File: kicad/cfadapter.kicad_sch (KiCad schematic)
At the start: 5 parts, among them CON1 CF-CARD, J1 Extension port, U1 GAL16V8

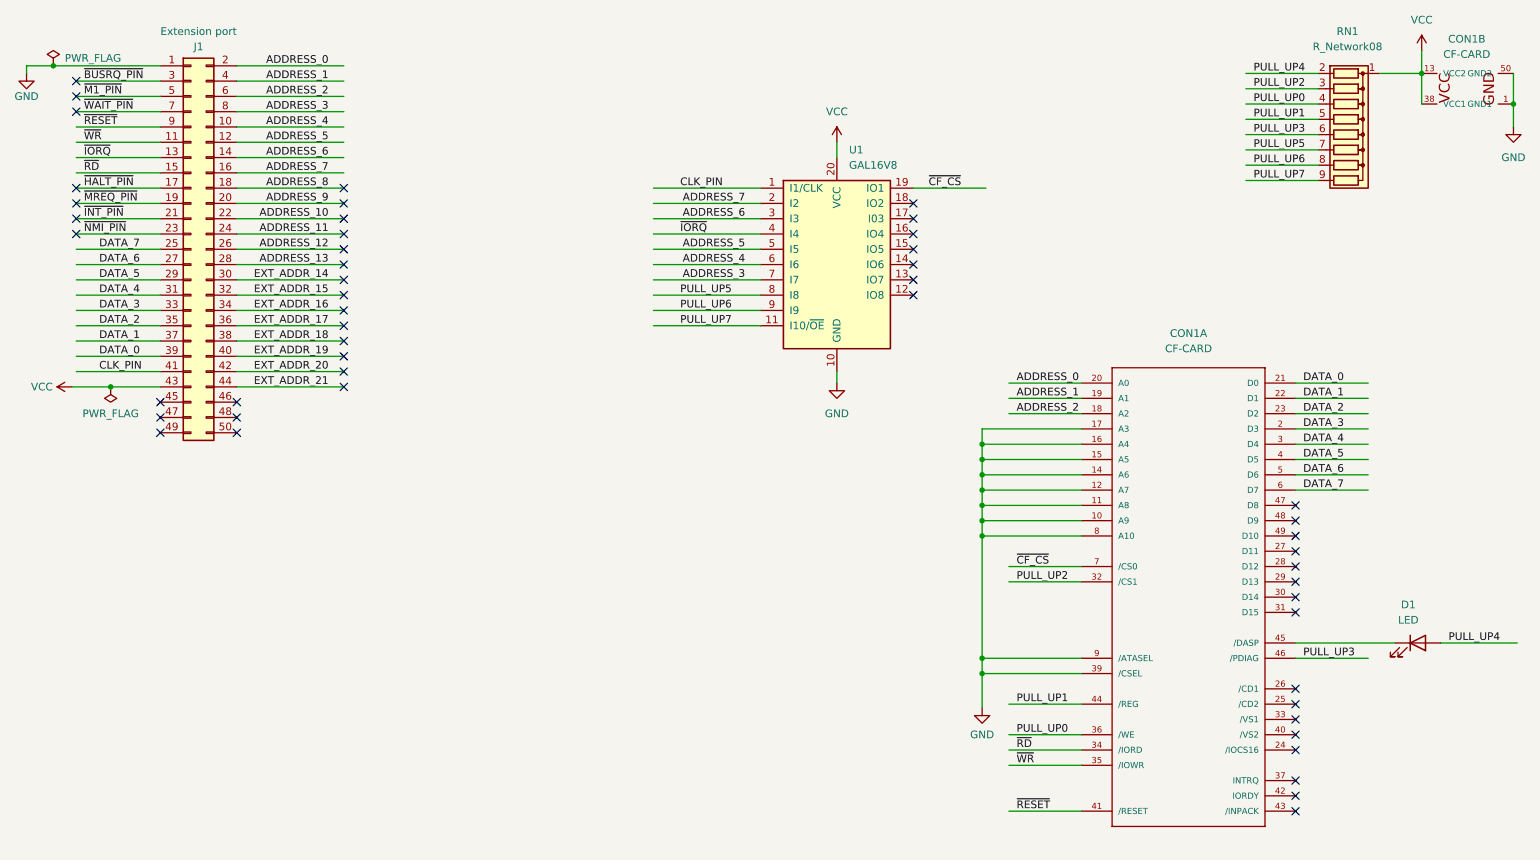
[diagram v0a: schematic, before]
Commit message: kicad: Update the PCB to the manufactured v1.0.0
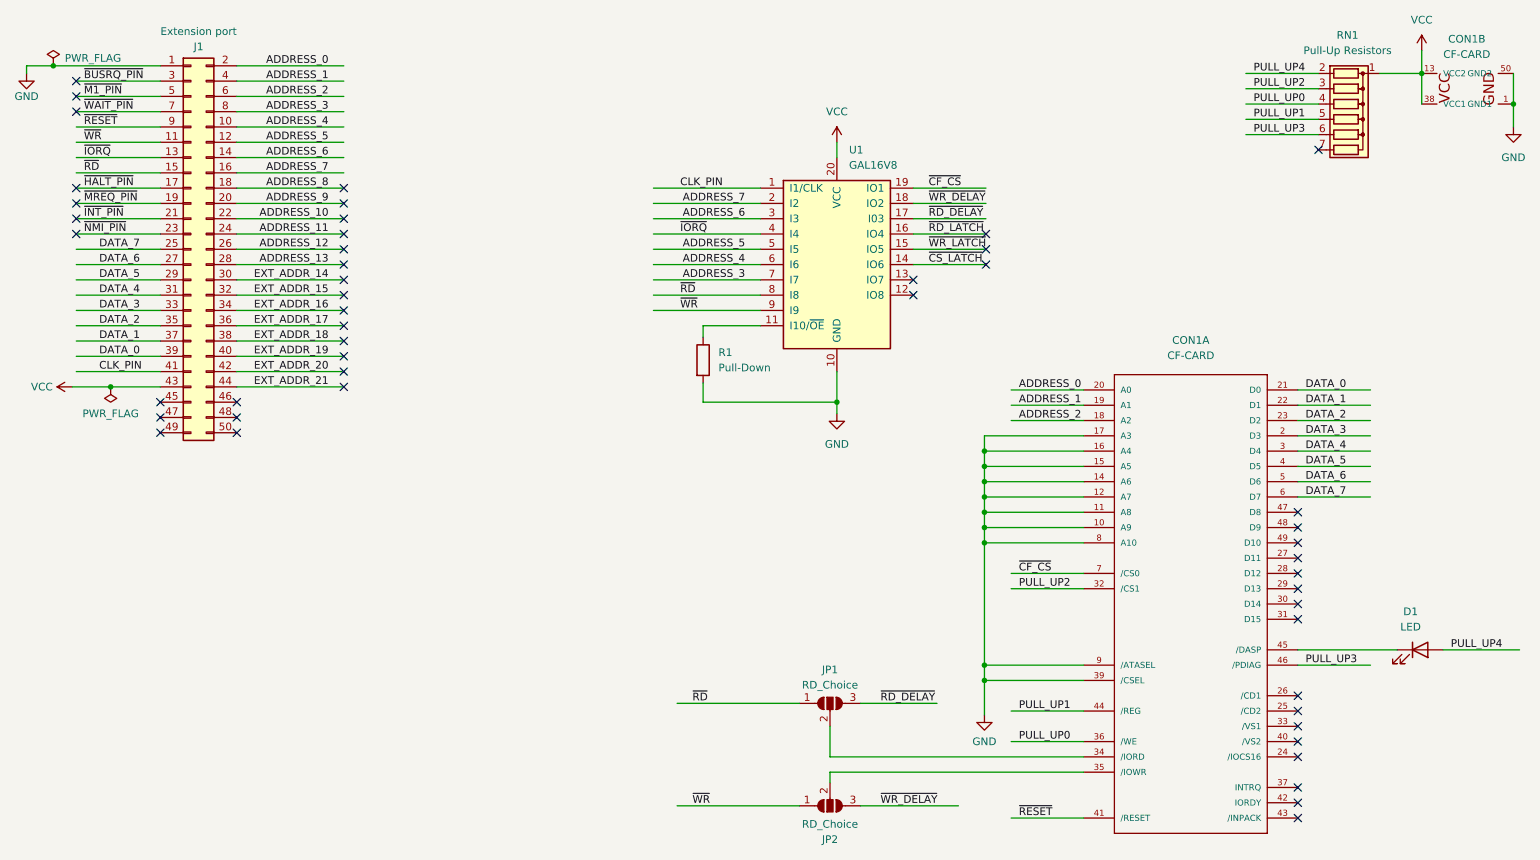
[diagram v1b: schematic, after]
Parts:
- added JP1, JP2: RD_Choice, Jumper:SolderJumper-3_P2.0mm_Open_TrianglePad1.0x1.5mm_NumberLabels, symbol Jumper:SolderJumper_3_Open
- added R1: Pull-Down, Resistor_THT:R_Axial_DIN0207_L6.3mm_D2.5mm_P10.16mm_Horizontal, symbol Device:R
- CON1: footprint Connector_Card:CF-Card_3M_N7E50-A516xx-30 -> Connector_Card:CF-Card_3M_N7E50-E516xx-30
- RN1: value R_Network08 -> Pull-Up Resistors; footprint Resistor_THT:R_Array_SIP9 -> Resistor_THT:R_Array_SIP7; symbol Device:R_Network08 -> Device:R_Network06
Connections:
- net GND: now also R1.2
- net ~{RD}: now also U1.8 (I8), JP1.1 (A); no longer CON1.34 (/IORD)
- net ~{WR}: now also U1.9 (I9), JP2.1 (A); no longer CON1.35 (/IOWR)
- net ~{CS_LATCH}: now reaches U1.14 (IO6)
- net ~{WR_LATCH}: now reaches U1.15 (IO5)
- net ~{RD_LATCH}: now reaches U1.16 (IO4)
- net ~{RD_DELAY}: now reaches U1.17 (I03)
- net ~{RD_DELAY}: now also JP1.3 (B)
- net ~{WR_DELAY}: now reaches U1.18 (IO2)
- net ~{WR_DELAY}: now also JP2.3 (B)
- net PULL_UP5: no longer names the net of RN1.7 (R6)
- net PULL_UP5: no longer U1.8 (I8)
- removed net PULL_UP6: RN1.8 (R7), U1.9 (I9)
- net PULL_UP7: no longer names the net of U1.11 (I10/~{OE})
- net PULL_UP7: now also R1.1; no longer RN1.9 (R8)
- new net: CON1.35 (/IOWR), JP2.2 (C)
- new net: CON1.34 (/IORD), JP1.2 (C)
- no-connect marks 50 -> 49
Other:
- moved on the sheet: CON1A, D1
